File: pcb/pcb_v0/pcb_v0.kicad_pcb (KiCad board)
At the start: 2 copper layers, 86 x 68 mm, 59 parts, among them J1 Conn_01x02_Pin, J2 Conn_01x02_Pin, J3 Conn_01x02_Pin, J4 Conn_01x02_Pin, U1 MAX3221EIPWR, U2 LM324, U3 XIAO-ESP32-C3-DIP

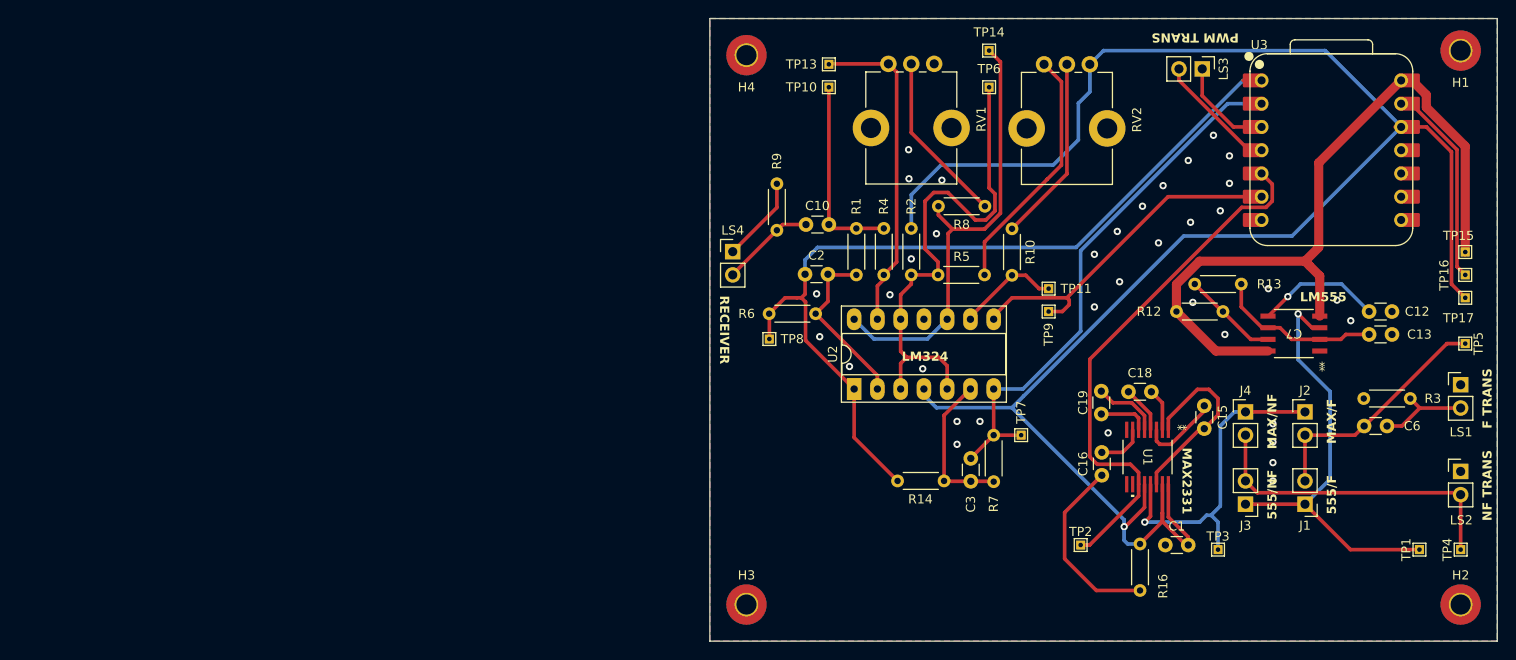
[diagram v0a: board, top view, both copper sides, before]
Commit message: fix(pcb): update design to match teacher requirements
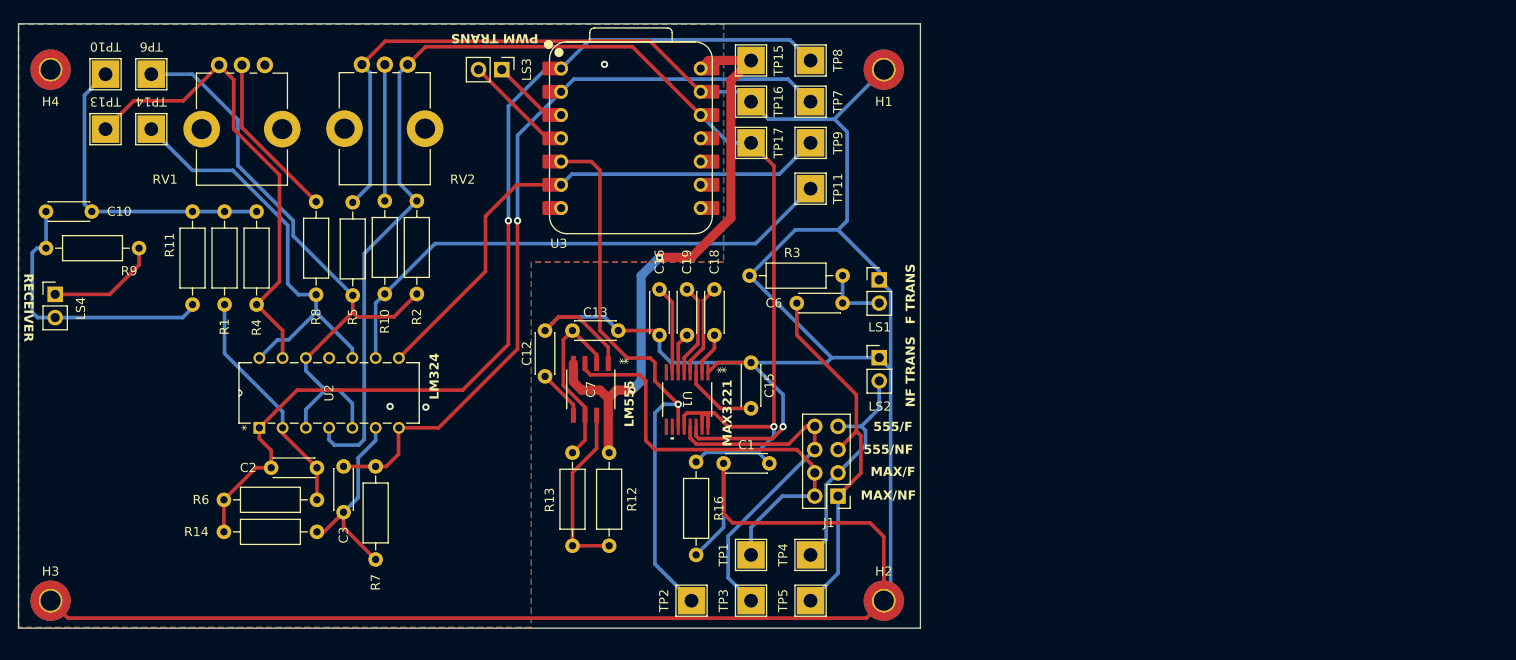
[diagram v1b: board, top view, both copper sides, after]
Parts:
- removed J2, J3, J4: Conn_01x02_Pin, Connector_PinHeader_2.54mm:PinHeader_1x02_P2.54mm_Vertical
- added R11: 0, Resistor_THT:R_Axial_DIN0207_L6.3mm_D2.5mm_P10.16mm_Horizontal, F.Cu at (123.0, 67.1)
- C1, C10, C12, C13, C15, C16, C18, C19, C2, C3, C6: footprint Capacitor_THT:C_Disc_D3.0mm_W1.6mm_P2.50mm -> Capacitor_THT:C_Disc_D4.3mm_W1.9mm_P5.00mm
- J1: value Conn_01x02_Pin -> Conn_02x04_Odd_Even; footprint Connector_PinHeader_2.54mm:PinHeader_1x02_P2.54mm_Vertical -> Connector_PinHeader_2.54mm:PinHeader_2x04_P2.54mm_Vertical
- R1, R10, R12, R13, R14, R16, R2, R3, R4, R5, R6, R7, R8, R9: footprint Resistor_THT:R_Axial_DIN0204_L3.6mm_D1.6mm_P5.08mm_Horizontal -> Resistor_THT:R_Axial_DIN0207_L6.3mm_D2.5mm_P10.16mm_Horizontal
- TP1, TP10, TP11, TP13, TP14, TP15, TP16, TP17, TP2, TP3, TP4, TP5, TP6, TP7, TP8, TP9: footprint TestPoint:TestPoint_THTPad_1.0x1.0mm_Drill0.5mm -> TestPoint:TestPoint_THTPad_3.0x3.0mm_Drill1.5mm
- U2: footprint Package_DIP:DIP-14_W7.62mm_Socket_LongPads -> LM324AN:N14
- moved C12 92.5 mm to (161.5, 80.1), turned to -90 degrees
- moved TP14 91.9 mm to (118.5, 58.1), turned to 180 degrees
- moved TP6 91.5 mm to (118.5, 52.1)
- moved C13 87.0 mm to (164.5, 80.1)
- moved C10 83.0 mm to (107.0, 67.1)
- moved TP15 80.8 mm to (184.0, 50.6), turned to 90 degrees
- moved TP16 80.3 mm to (184.0, 55.1), turned to 90 degrees
- moved TP17 79.8 mm to (184.0, 59.6), turned to 90 degrees
- moved TP13 79.3 mm to (113.5, 58.1), turned to 180 degrees
- moved TP10 79.0 mm to (113.5, 52.1), turned to 180 degrees
- moved C7 77.0 mm to (166.5, 86.5), turned to -90 degrees
- moved TP5 76.8 mm to (190.5, 109.6)
- moved U3 76.5 mm to (171.0, 59.1)
- moved LS3 76.5 mm to (156.8, 51.6)
- moved H4 76.0 mm to (107.5, 51.6)
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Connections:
- J1 pad 1: 555_PULSE -> emit_f
- J1 pad 2: emit_f -> 555_PULSE
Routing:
- net GND: track 91.6 -> 373.3 mm, vias 36 -> 4
- net +3.3V: track 208.2 -> 152.3 mm
- net Net-(U2C--): track 11.3 -> 58.7 mm
- net aop_stage_2_out: track 58.9 -> 84.7 mm, vias 0 -> 1
- net Net-(C10-Pad1): track 10.3 -> 30.7 mm
- net comparator_out: track 38.4 -> 58.2 mm
- net +5V: track 82.9 -> 64.8 mm, vias 0 -> 2
- net Net-(U2D--): track 35.7 -> 52.8 mm
- net emit_f: track 26.6 -> 40.5 mm
- net trans_rcv: track 21.2 -> 34.3 mm
- net aop_offset: track 55.8 -> 68.8 mm
- net aop_stage_1_out: track 96.1 -> 108.9 mm, vias 0 -> 1
- net emit_nf: track 35.1 -> 25.0 mm
- net Net-(C7-DIS): track 10.5 -> 19.3 mm
- net Net-(C7-CVOLT): track 13.7 -> 5.53 mm, vias 1 -> 0
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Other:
- board size 86 x 68 mm -> 98.5 x 66 mm
- board text added: "MAX3221"
- board text removed: "MAX2331"
